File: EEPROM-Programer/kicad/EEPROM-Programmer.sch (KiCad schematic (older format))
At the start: 8 parts, among them U1 74HC595, U2 74HC595, U3 28C256

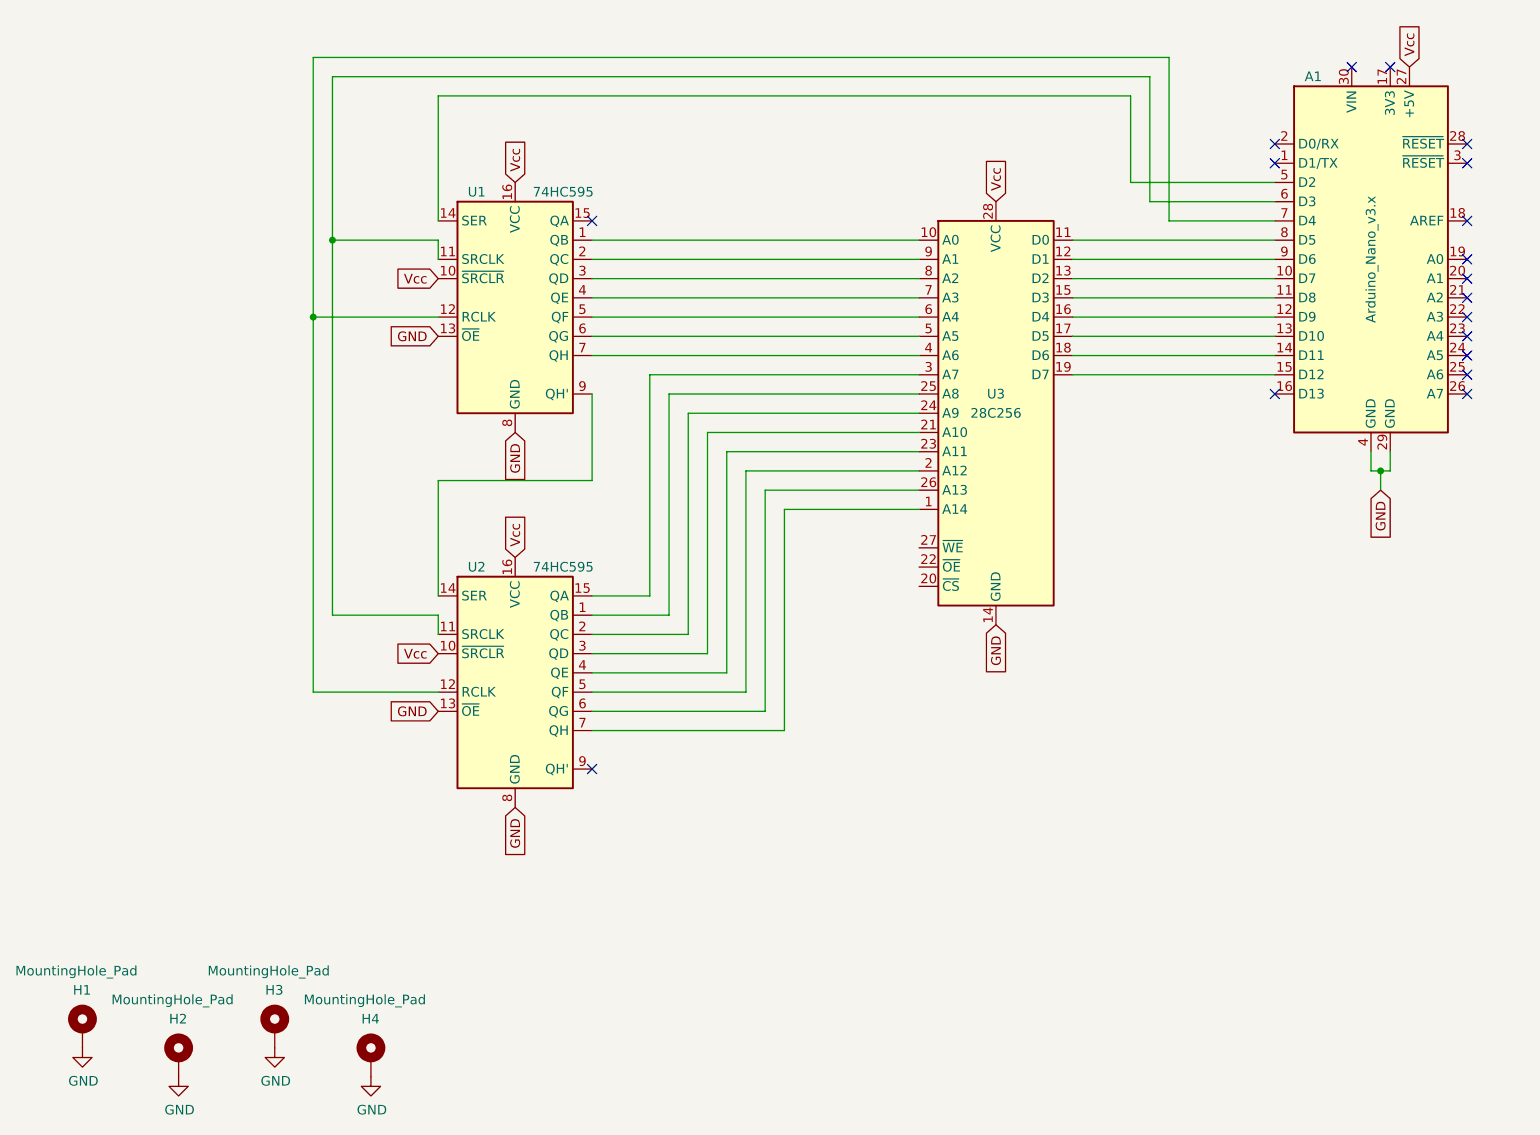
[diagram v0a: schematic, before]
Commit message: EEPROM Programmer: New circuit, with more flexibility
Redesigned the circuit to be able to control the OE, CS and WE pins from the
EEPROM, and the OE, SRCLR pins from the shift register.

This gives us more total control of all the pins in both chips, and
enables us to write to the EEPROM (before the WE pin was always HIGH).

I also added a status LED for monitoring.
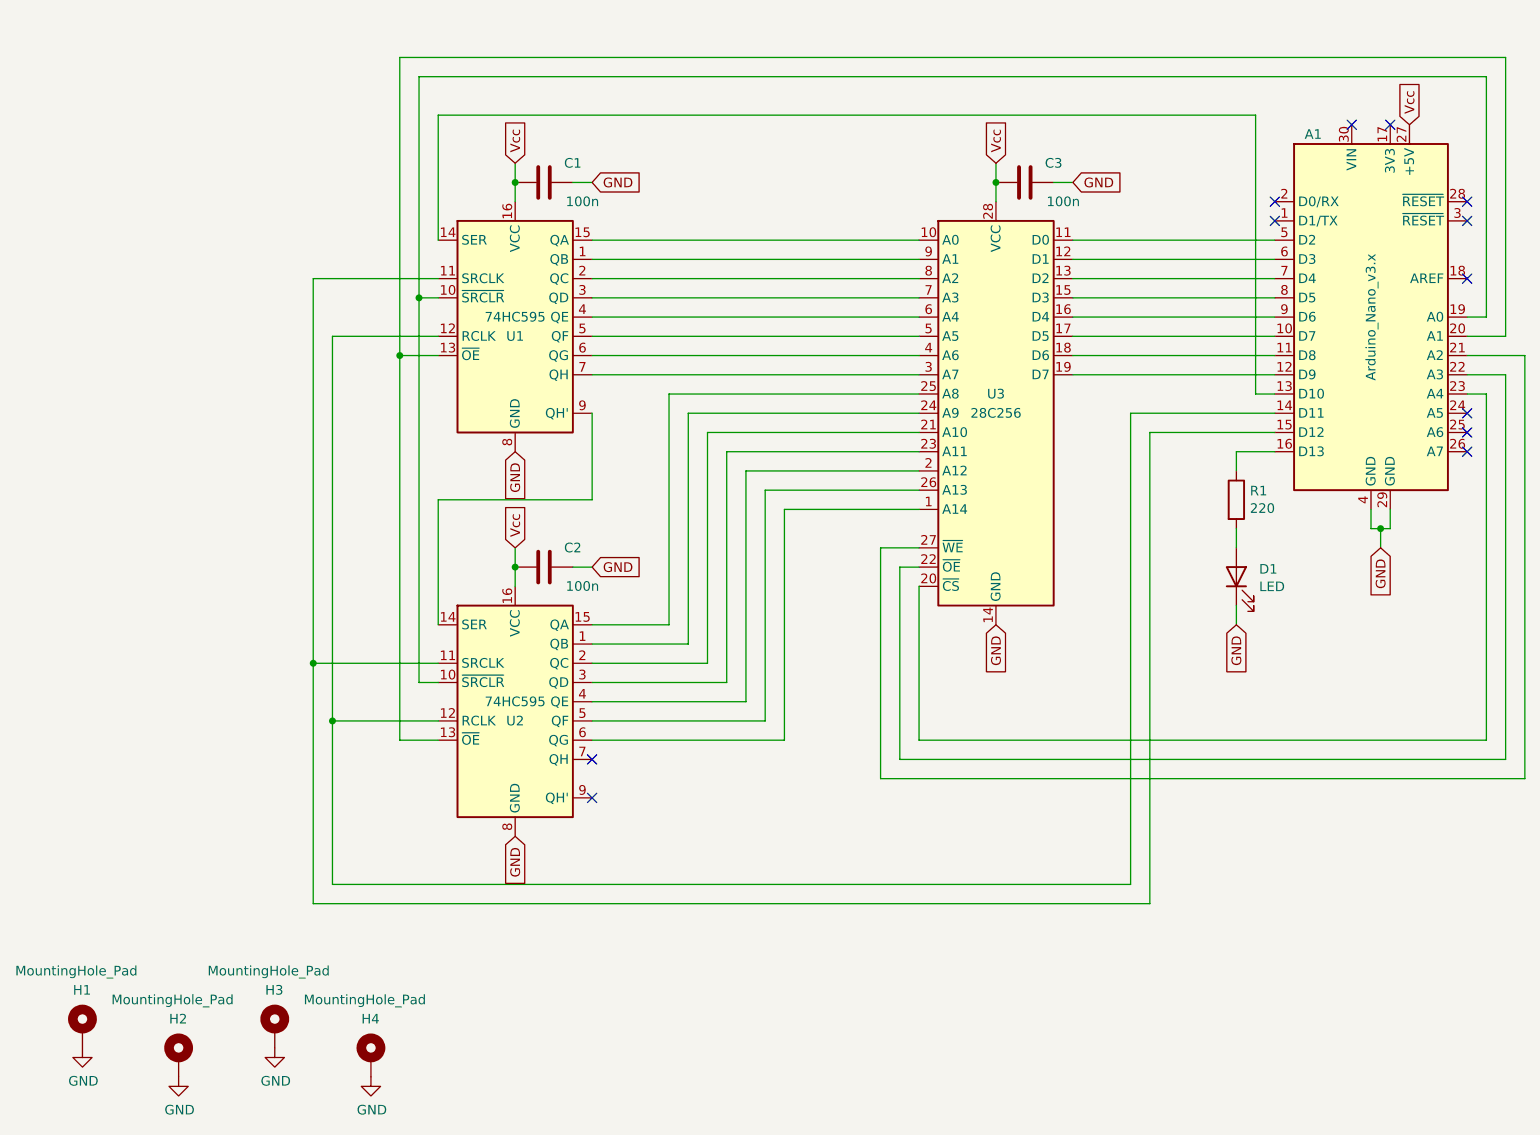
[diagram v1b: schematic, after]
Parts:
- added C1, C2, C3: 100n, Capacitor_THT:C_Disc_D4.7mm_W2.5mm_P5.00mm, symbol Device:C
- added D1: LED, LED_THT:LED_D3.0mm, symbol Device:LED
- added R1: 220, Resistor_THT:R_Axial_DIN0204_L3.6mm_D1.6mm_P7.62mm_Horizontal, symbol Device:R
- U3: footprint Package_DIP:DIP-28_W15.24mm_Socket -> Socket:DIP_Socket-28_W11.9_W12.7_W15.24_W17.78_W18.5_3M_228-1277-00-0602J
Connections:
- net GND: now also C1.1, C2.1, C3.1, D1.1 (K); no longer U1.13 (~OE), U2.13 (~OE)
- net Vcc: now also C1.2, C2.2, C3.2; no longer U1.10 (~SRCLR), U2.10 (~SRCLR)
- net at U1.1 (QB): now also U3.9 (A1); no longer U3.10 (A0)
- net at U1.11 (SRCLK), U2.11 (SRCLK): now also A1.15 (D12); no longer A1.6 (D3)
- net at U1.12 (RCLK), U2.12 (RCLK): now also A1.14 (D11); no longer A1.7 (D4)
- net at U1.14 (SER): now also A1.13 (D10); no longer A1.5 (D2)
- net at U1.15 (QA): now also U3.10 (A0)
- net at U1.2 (QC): now also U3.8 (A2); no longer U3.9 (A1)
- net at U1.3 (QD): now also U3.7 (A3); no longer U3.8 (A2)
- net at U1.4 (QE): now also U3.6 (A4); no longer U3.7 (A3)
- net at U1.5 (QF): now also U3.5 (A5); no longer U3.6 (A4)
- net at U1.6 (QG): now also U3.4 (A6); no longer U3.5 (A5)
- net at U1.7 (QH): now also U3.3 (A7); no longer U3.4 (A6)
- net at U2.1 (QB): now also U3.24 (A9); no longer U3.25 (A8)
- net at U2.15 (QA): now also U3.25 (A8); no longer U3.3 (A7)
- net at U2.2 (QC): now also U3.21 (A10); no longer U3.24 (A9)
- net at U2.3 (QD): now also U3.23 (A11); no longer U3.21 (A10)
- net at U2.4 (QE): now also U3.2 (A12); no longer U3.23 (A11)
- net at U2.5 (QF): now also U3.26 (A13); no longer U3.2 (A12)
- net at U2.6 (QG): now also U3.1 (A14); no longer U3.26 (A13)
- net at U2.7 (QH): no longer U3.1 (A14)
- net at U3.11 (D0): now also A1.5 (D2); no longer A1.8 (D5)
- net at U3.12 (D1): now also A1.6 (D3); no longer A1.9 (D6)
- net at U3.13 (D2): now also A1.7 (D4); no longer A1.10 (D7)
- net at U3.15 (D3): now also A1.8 (D5); no longer A1.11 (D8)
- net at U3.16 (D4): now also A1.9 (D6); no longer A1.12 (D9)
- net at U3.17 (D5): now also A1.10 (D7); no longer A1.13 (D10)
- net at U3.18 (D6): now also A1.11 (D8); no longer A1.14 (D11)
- net at U3.19 (D7): now also A1.12 (D9); no longer A1.15 (D12)
- net at U3.20 (~CS): now also A1.23 (A4)
- net at U3.22 (~OE): now also A1.22 (A3)
- net at U3.27 (~WE): now also A1.21 (A2)
- net at A1.16 (D13): now also R1.1
- net at A1.19 (A0): now also U1.10 (~SRCLR), U2.10 (~SRCLR)
- net at A1.20 (A1): now also U1.13 (~OE), U2.13 (~OE)
- new net: D1.2 (A), R1.2
- no-connect marks 18 -> 12
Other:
- moved on the sheet: A1, U1, U2
